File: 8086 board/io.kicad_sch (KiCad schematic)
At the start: 80 parts, among them J2 RM68090, J3 RGB LCD, U22 74AC573, U23 74AC573, U24 74AC573, U25 74AC573, U26 74AC573, U27 74AC573, U28 74AC573, U29 74AC573, U30 74LVC245A, U31 74LVC245A, U32 74LVC245A, U4 74HC02, U5 74HC02

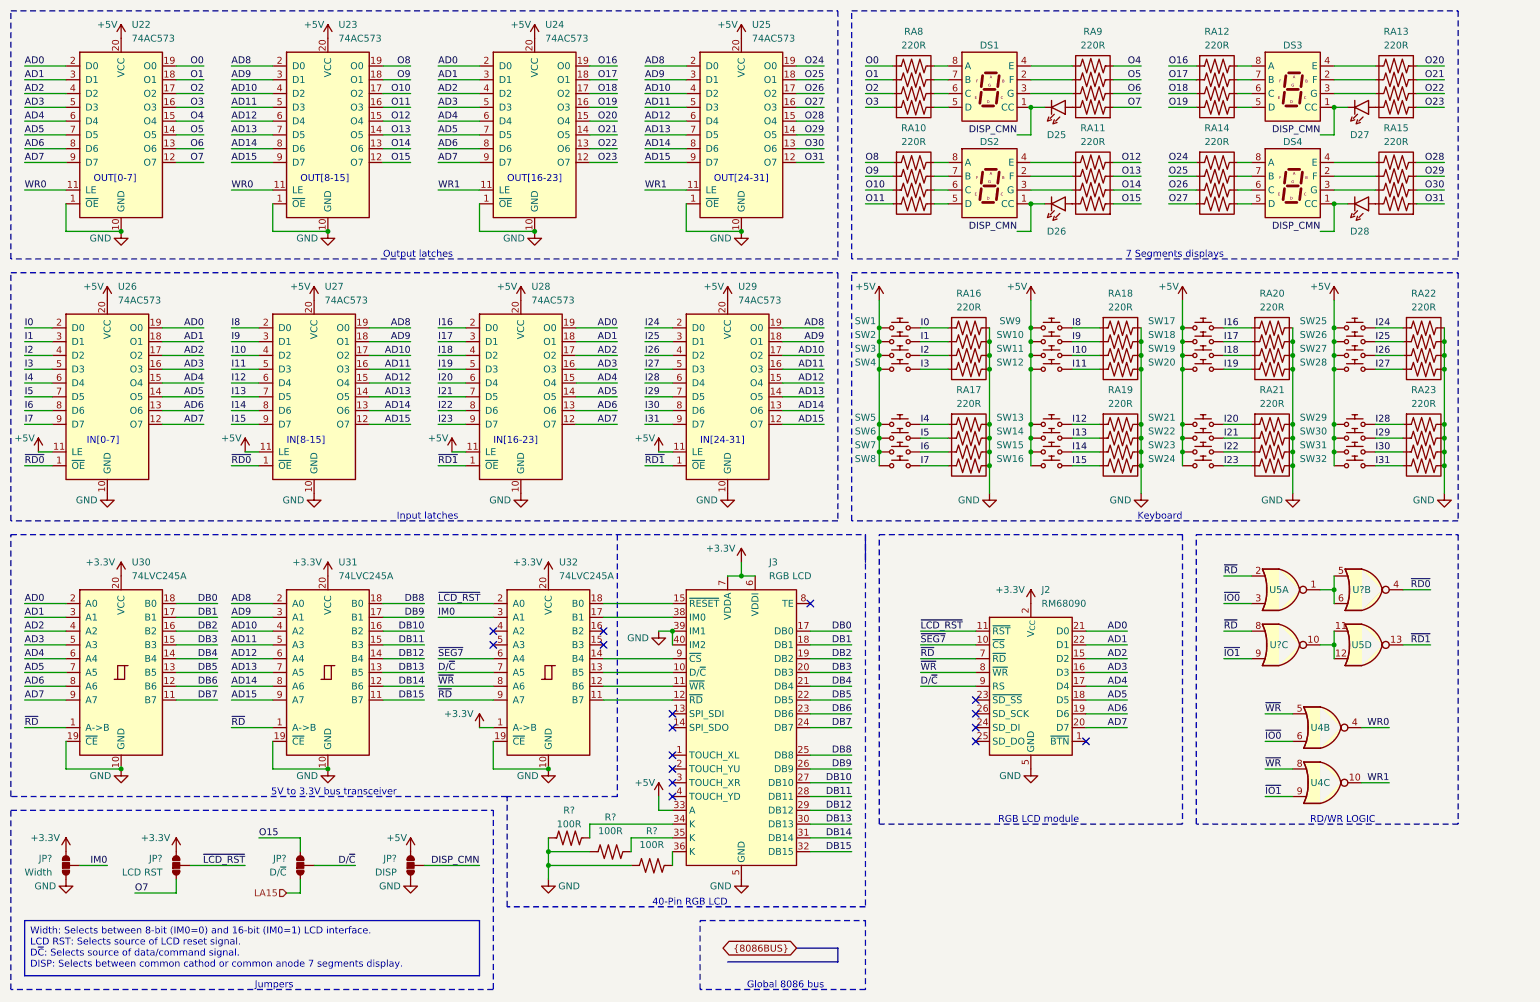
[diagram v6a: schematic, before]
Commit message: change schematic to use new components
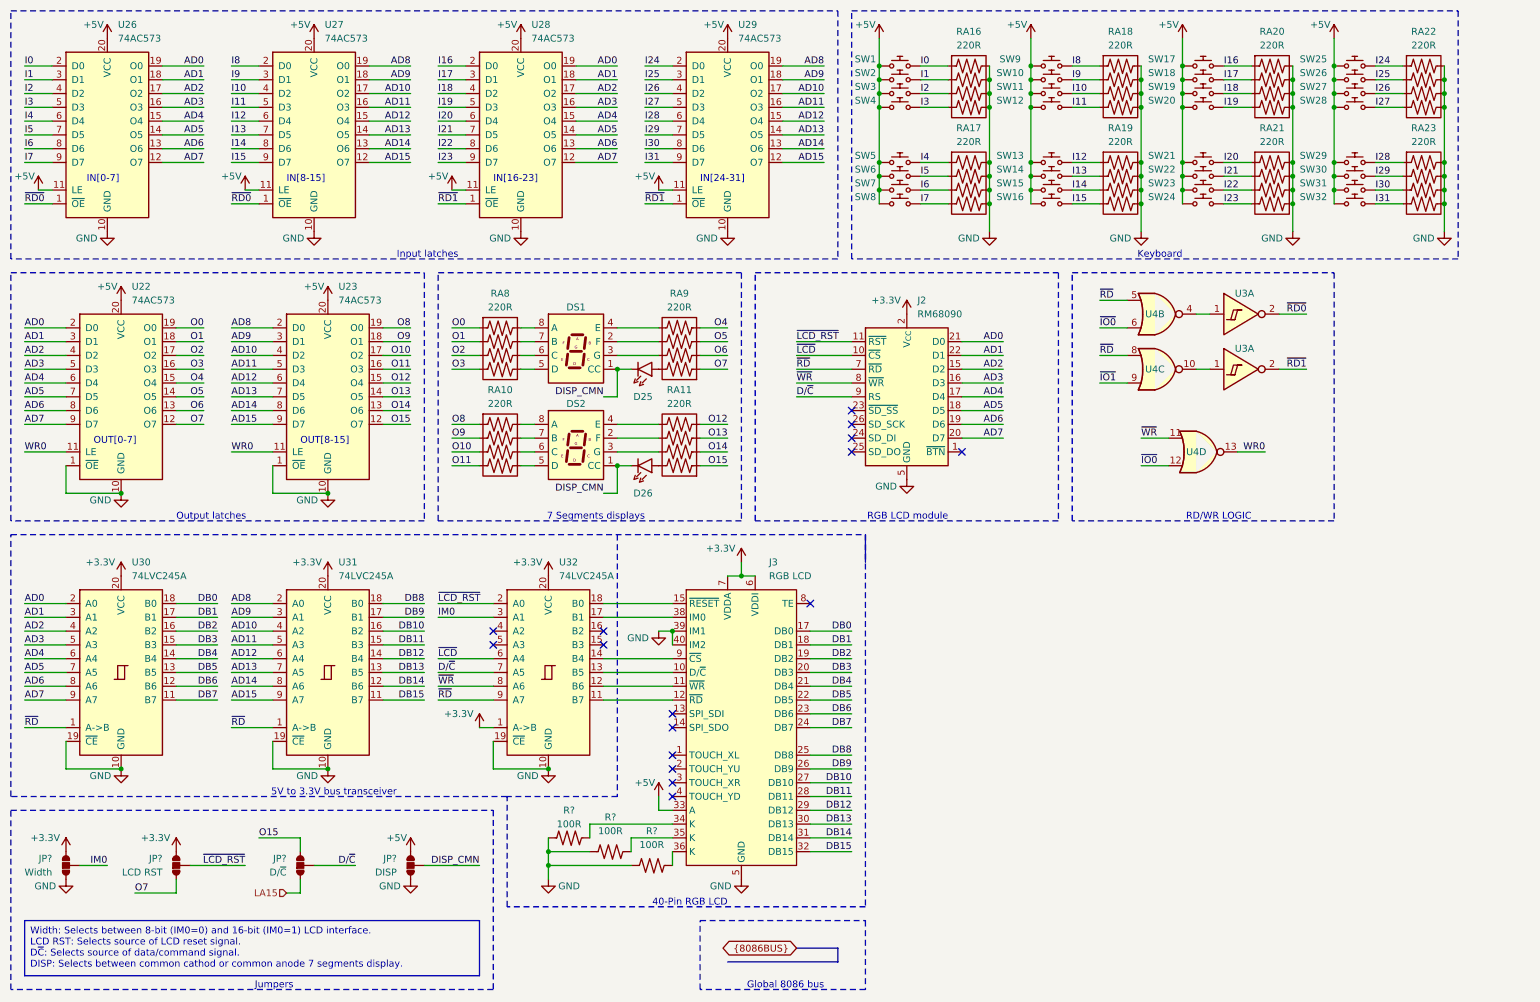
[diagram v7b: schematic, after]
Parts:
- removed D27, D28: LED, LED_SMD:LED_0603_1608Metric_Pad1.05x0.95mm_HandSolder, symbol 8086PC:LED
- removed DS3, DS4: 7SEG, 8086PC:2181AS, symbol 8086PC:2181AS
- removed RA12, RA13, RA14, RA15: 220R, Resistor_SMD:R_Array_Concave_4x0603, symbol 8086PC:R_Array_4
- removed U24, U25: 74AC573, Package_SO:TSSOP-20_4.4x6.5mm_P0.65mm, symbol 8086PC:74AC573
- removed U5, U? (x2): 74HC02, Package_SO:SOIC-14_3.9x8.7mm_P1.27mm, symbol 8086PC:74HC02
- added U3 (x2): 74HC14, Package_SO:SOIC-14_3.9x8.7mm_P1.27mm, symbol 8086PC:74HC14
- added unit 4 of U4
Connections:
- net WR0: now also U4.13; no longer U4.4
- net ~{IO0}: now also U4.12
- net ~{RD0}: now also U3.2
- net ~{RD1}: now also U3.2
- net ~{RD}: now also U4.5, U4.8
- net ~{WR}: now also U4.11; no longer U4.5, U4.8
- net WR1: no longer names the net of U4.10
- net WR1: now also U3.1
- net ~{SEG7} renamed ~{LCD}
- new net: U3.1, U4.4
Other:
- note removed: "OUT[16-23]"
- note removed: "OUT[24-31]"
- moved on the sheet: D25, D26, DS1, DS2, J2, RA10, RA11, RA16, RA17, RA18, RA19, RA20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
